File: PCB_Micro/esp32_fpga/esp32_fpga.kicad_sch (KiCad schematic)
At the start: 88 parts, among them IC1 ICE40UP5K-SG48I, J1 DM3AT-SF-PEJM5, J2 AUX1, J3 USB_C_Receptacle_USB2.0_16P, J4 Conn_01x04_Pin, J7 AUX2, J8 AUX3, Q1 DMP1045U-7, SW1 SW_Push, U1 ESP32-S3-WROOM-1-N8R8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

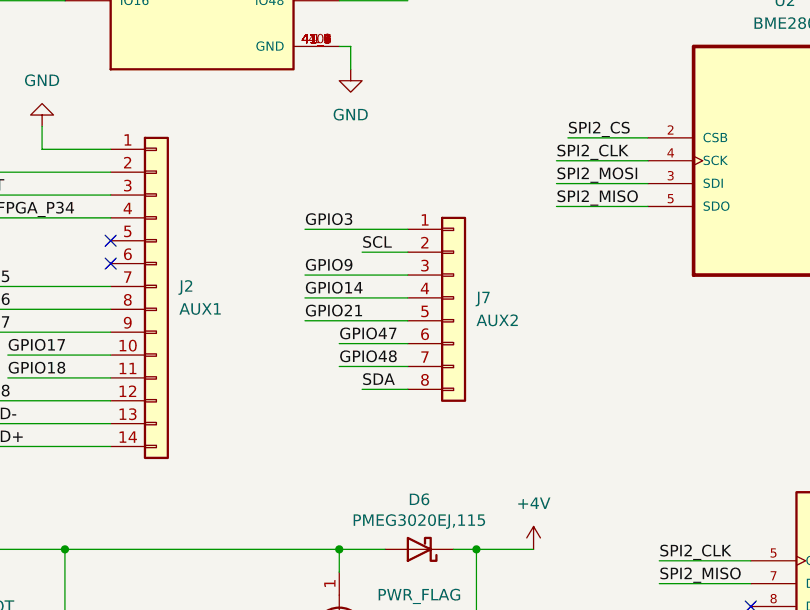
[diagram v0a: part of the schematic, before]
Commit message: PCB save agencement esp32
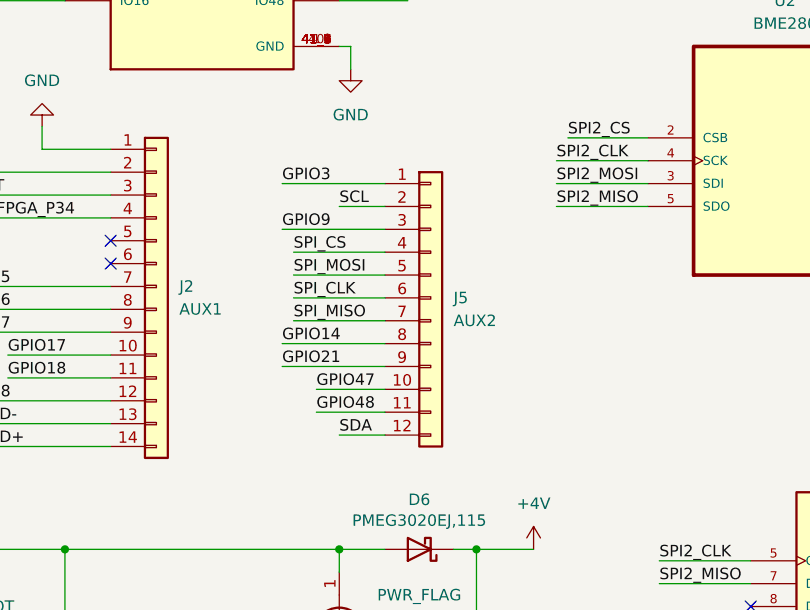
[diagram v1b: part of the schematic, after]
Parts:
- removed J7: AUX2, Connector_PinSocket_1.27mm:PinSocket_1x08_P1.27mm_Vertical, symbol Connector_Generic:Conn_01x08
- added J5: AUX2, Connector_PinSocket_1.00mm:PinSocket_1x12_P1.00mm_Vertical, symbol Connector_Generic:Conn_01x12
- TP1: value TestPoint -> SPI_MISO
- TP2: value TestPoint -> SPI_CLK
- TP3: value TestPoint -> SPI_CS
- TP4: value TestPoint -> SPI_MOSI
- TP5: value TestPoint -> CDONE
- TP6: value TestPoint -> CRESET
- TP7: value TestPoint -> VBATT
- TP8: value TestPoint -> GND
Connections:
- net GPIO14: now also J5.8 (Pin_8)
- net GPIO21: now also J5.9 (Pin_9)
- net GPIO3: now also J5.1 (Pin_1)
- net GPIO47: now also J5.10 (Pin_10)
- net GPIO48: now also J5.11 (Pin_11)
- net GPIO9: now also J5.3 (Pin_3)
- net SCL: now also J5.2 (Pin_2)
- net SDA: now also J5.12 (Pin_12)
- net SPI_CLK: now also J5.6 (Pin_6)
- net SPI_CS: now also J5.4 (Pin_4)
- net SPI_MISO: now also J5.7 (Pin_7)
- net SPI_MOSI: now also J5.5 (Pin_5)

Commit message: PCB presque terminé
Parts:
- added D8: LED_RGB, LED_SMD:LED_RGB_5050-6, symbol Device:LED_RGB
- J4: footprint Connector:NS-Tech_Grove_1x04_P2mm_Vertical -> Connector_PinHeader_2.00mm:PinHeader_1x04_P2.00mm_Vertical_SMD_Pin1Left
- TP1, TP2, TP3, TP4: footprint TestPoint:TestPoint_Pad_D1.0mm -> TestPoint:TestPoint_THTPad_1.0x1.0mm_Drill0.5mm
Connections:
- net PIN_P10: now also MK1.3 (WS)
- net PIN_P2: no longer MK1.1 (SCK)
- net PIN_P3: no longer MK1.2 (SD)
- net PIN_P4: no longer MK1.3 (WS)
- net PIN_P6: now also MK1.1 (SCK)
- net PIN_P9: now also MK1.2 (SD)
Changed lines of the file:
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@@
 		)
 	)
-	(label "PIN_P3"
+	(label "PIN_P9"
 		(at 265.43 40.64 180)
 		(effects
@@
 		)
 	)
-	(label "PIN_P4"
+	(label "PIN_P10"
 		(at 265.43 43.18 180)
 		(effects
@@
 		)
 	)
-	(label "PIN_P2"
+	(label "PIN_P6"
 		(at 265.43 38.1 180)
 		(effects
@@
 			)
 		)
-		(property "Footprint" "TestPoint:TestPoint_Pad_D1.0mm"
+		(property "Footprint" "TestPoint:TestPoint_THTPad_1.0x1.0mm_Drill0.5mm"
 			(at 234.95 252.73 0)
 			(effects
@@
 			)
 		)
-		(property "Footprint" "TestPoint:TestPoint_Pad_D1.0mm"
+		(property "Footprint" "TestPoint:TestPoint_THTPad_1.0x1.0mm_Drill0.5mm"
 			(at 234.95 247.65 0)
 			(effects
@@
 			)
 		)
-		(property "Footprint" "Connector:NS-Tech_Grove_1x04_P2mm_Vertical"
+		(property "Footprint" "Connector_PinHeader_2.00mm:PinHeader_1x04_P2.00mm_Vertical_SMD_Pin1Left"
 			(at 138.43 87.63 0)
 			(effects
@@
 	)
 	(symbol
+		(lib_id "Device:LED_RGB")
+		(at 351.79 220.98 0)
+		(unit 1)
+		(exclude_from_sim no)
+		(in_bom yes)
+		(on_board yes)
+		(dnp no)
+		(fields_autoplaced yes)
+		(property "Reference" "D8"
+			(at 351.79 207.01 0)
+			(effects
+				(font
+					(size 1.27 1.27)
+				)
+			)
+		)
+		(property "Value" "LED_RGB"
+			(at 351.79 209.55 0)
+			(effects
+				(font
+					(size 1.27 1.27)
+				)
+			)
+		)
+		(property "Footprint" "LED_SMD:LED_RGB_5050-6"
+			(at 351.79 222.25 0)
+			(effects
+				(font
+					(size 1.27 1.27)
+				)
+				(hide yes)
+			)
+		)
+		(property "Datasheet" "~"
+			(at 351.79 222.25 0)
+			(effects
+				(font
+					(size 1.27 1.27)
+				)
+				(hide yes)
+			)
+		)
+		(property "Description" "RGB LED, 6 pin package"
+			(at 351.79 220.98 0)
+			(effects
+				(font
+					(size 1.27 1.27)
+				)
+				(hide yes)
+			)
+		)
+		(pin "3"
+		)
+		(pin "1"
+		)
+		(pin "6"
+		)
+		(pin "5"
+		)
+		(pin "4"
+		)
+		(pin "2"
+		)
+		(instances
+			(project ""
+				(path "/e9b45eef-13aa-420c-803d-e39bf82057f5"
+					(reference "D8")
+					(unit 1)
+				)
+			)
+		)
+	)
+	(symbol
 		(lib_id "power:+3.3V")
 		(at 330.2 22.86 0)
@@
 			)
 		)
-		(property "Footprint" "TestPoint:TestPoint_Pad_D1.0mm"
+		(property "Footprint" "TestPoint:TestPoint_THTPad_1.0x1.0mm_Drill0.5mm"
 			(at 234.95 250.19 0)
 			(effects
@@
 			)
 		)
-		(property "Footprint" "TestPoint:TestPoint_Pad_D1.0mm"
+		(property "Footprint" "TestPoint:TestPoint_THTPad_1.0x1.0mm_Drill0.5mm"
 			(at 234.95 245.11 0)
 			(effects

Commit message: PCB rooté reste les erreurs a voir
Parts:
- removed J1: DM3AT-SF-PEJM5, custom:HRS_DM3AT-SF-PEJM5, symbol DM3AT-SF-PEJM5:DM3AT-SF-PEJM5
- removed TP1: SPI_MISO, TestPoint:TestPoint_THTPad_1.0x1.0mm_Drill0.5mm, symbol Connector:TestPoint
- removed TP2: SPI_CLK, TestPoint:TestPoint_THTPad_1.0x1.0mm_Drill0.5mm, symbol Connector:TestPoint
- removed TP3: SPI_CS, TestPoint:TestPoint_THTPad_1.0x1.0mm_Drill0.5mm, symbol Connector:TestPoint
- removed TP4: SPI_MOSI, TestPoint:TestPoint_THTPad_1.0x1.0mm_Drill0.5mm, symbol Connector:TestPoint
- removed TP5: CDONE, TestPoint:TestPoint_Pad_D1.0mm, symbol Connector:TestPoint
- removed TP6: CRESET, TestPoint:TestPoint_Pad_D1.0mm, symbol Connector:TestPoint
- added J6: 503398-1892, custom:5033981892, symbol 503398-1892:503398-1892
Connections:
- net +3.3V: now also J6.4 (VDD)
- net ADC: now also J2.4 (Pin_4)
- net CDONE: now also J2.8 (Pin_8)
- net CRESET: now also J2.9 (Pin_9)
- net GND: now also J6.11, J6.12, J6.13, J6.14, J6.6 (VSS)
- net GPIO5: now also J2.5 (Pin_5); no longer J2.7 (Pin_7)
- net GPIO6: now also J2.6 (Pin_6); no longer J2.8 (Pin_8)
- net GPIO7: now also J2.7 (Pin_7); no longer J2.9 (Pin_9)
- net SPI2_CLK: now also J6.5 (CLK)
- net SPI2_CS: now also J6.2 (CD/DAT3)
- net SPI2_MISO: now also J6.7 (DAT0)
- net SPI2_MOSI: now also J6.3 (CMD)
- net FPGA_P34: no longer names the net of IC1.34 (IOT_44B)
- net FPGA_P34: no longer J2.4 (Pin_4)
- no-connect marks 8 -> 7
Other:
- moved on the sheet: C11

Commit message: PCB terminé avec gerber sans LEDs niveau sonore
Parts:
- added SW2: SW_Push, Button_Switch_SMD:SW_SPST_PTS810, symbol Switch:SW_Push
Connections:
- net GND: now also SW2.2
- net GPIO0: now also SW2.1
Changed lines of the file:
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@@
 	(wire
 		(pts
+			(xy 25.4 53.34) (xy 25.4 57.15)
+		)
+		(stroke
+			(width 0)
+			(type default)
+		)
+	)
+	(wire
+		(pts
 			(xy 162.56 127) (xy 163.83 127)
 		)
@@
 	(wire
 		(pts
+			(xy 25.4 67.31) (xy 25.4 72.39)
+		)
+		(stroke
+			(width 0)
+			(type default)
+		)
+	)
+	(wire
+		(pts
 			(xy 62.23 133.35) (xy 72.39 133.35)
 		)
@@
 		)
 	)
+	(label "GPIO0"
+		(at 25.4 53.34 0)
+		(effects
+			(font
+				(size 1.27 1.27)
+			)
+			(justify left bottom)
+		)
+	)
 	(label "PIN_P48"
 		(at 201.93 72.39 180)
@@
 	)
 	(symbol
+		(lib_id "power:GND")
+		(at 25.4 72.39 0)
+		(mirror y)
+		(unit 1)
+		(exclude_from_sim no)
+		(in_bom yes)
+		(on_board yes)
+		(dnp no)
+		(property "Reference" "#PWR014"
+			(at 25.4 78.74 0)
+			(effects
+				(font
+					(size 1.27 1.27)
+				)
+				(hide yes)
+			)
+		)
+		(property "Value" "GND"
+			(at 25.273 76.7842 0)
+			(effects
+				(font
+					(size 1.27 1.27)
+				)
+			)
+		)
+		(property "Footprint" ""
+			(at 25.4 72.39 0)
+			(effects
+				(font
+					(size 1.27 1.27)
+				)
+				(hide yes)
+			)
+		)
+		(property "Datasheet" ""
+			(at 25.4 72.39 0)
+			(effects
+				(font
+					(size 1.27 1.27)
+				)
+				(hide yes)
+			)
+		)
+		(property "Description" ""
+			(at 25.4 72.39 0)
+			(effects
+				(font
+					(size 1.27 1.27)
+				)
+			)
+		)
+		(pin "1"
+		)
+		(instances
+			(project "esp32_fpga"
+				(path "/e9b45eef-13aa-420c-803d-e39bf82057f5"
+					(reference "#PWR014")
+					(unit 1)
+				)
+			)
+		)
+	)
+	(symbol
 		(lib_id "Device:LED_Small")
 		(at 213.36 182.88 90)
@@
 					(unit 1)
 				)
+			)
+		)
+	)
+	(symbol
+		(lib_id "Switch:SW_Push")
+		(at 25.4 62.23 90)
+		(mirror x)
+		(unit 1)
+		(exclude_from_sim no)
+		(in_bom yes)
+		(on_board yes)
+		(dnp no)
+		(property "Reference" "SW2"
+			(at 20.32 62.23 0)
+			(effects
+				(font
+					(size 1.27 1.27)
+				)
+			)
+		)
+		(property "Value" "SW_Push"
+			(at 20.4724 62.23 0)
+			(effects
+				(font
+					(size 1.27 1.27)
+				)
+				(hide yes)
+			)
+		)
+		(property "Footprint" "Button_Switch_SMD:SW_SPST_PTS810"
+			(at 20.32 62.23 0)
+			(effects
+				(font
+					(size 1.27 1.27)
+				)
+				(hide yes)
+			)
+		)
+		(property "Datasheet" "~"
+			(at 20.32 62.23 0)
+			(effects
+				(font
+					(size 1.27 1.27)
+				)
+				(hide yes)
+			)
+		)
+		(property "Description" ""
+			(at 25.4 62.23 0)
+			(effects
+				(font
+					(size 1.27 1.27)
+				)
+			)
+		)
+		(pin "1"
+		)
+		(pin "2"
+		)
+		(instances
+			(project "esp32_fpga"
+				(path "/e9b45eef-13aa-420c-803d-e39bf82057f5"
+					(reference "SW2")
+					(unit 1)
+				)

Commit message: Ajout de labels et modifications d'empreinte tjr sans LED
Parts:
- J4: footprint Connector_PinHeader_2.00mm:PinHeader_1x04_P2.00mm_Vertical_SMD_Pin1Left -> Connector_PinSocket_2.54mm:PinSocket_1x04_P2.54mm_Vertical
- PMOD1, PMOD2, PMOD3: footprint Connector_PinSocket_2.54mm:PinSocket_2x06_P2.54mm_Vertical -> Connector_Samtec_HLE_THT:Samtec_HLE-106-02-xx-DV-TE_2x06_P2.54mm_Horizontal
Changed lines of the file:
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@@
 			)
 		)
-		(property "Footprint" "Connector_PinSocket_2.54mm:PinSocket_2x06_P2.54mm_Vertical"
+		(property "Footprint" "Connector_Samtec_HLE_THT:Samtec_HLE-106-02-xx-DV-TE_2x06_P2.54mm_Horizontal"
 			(at 207.01 138.43 0)
 			(effects
@@
 			)
 		)
-		(property "Footprint" "Connector_PinSocket_2.54mm:PinSocket_2x06_P2.54mm_Vertical"
+		(property "Footprint" "Connector_Samtec_HLE_THT:Samtec_HLE-106-02-xx-DV-TE_2x06_P2.54mm_Horizontal"
 			(at 271.78 100.33 0)
 			(effects
@@
 			)
 		)
-		(property "Footprint" "Connector_PinHeader_2.00mm:PinHeader_1x04_P2.00mm_Vertical_SMD_Pin1Left"
+		(property "Footprint" "Connector_PinSocket_2.54mm:PinSocket_1x04_P2.54mm_Vertical"
 			(at 138.43 87.63 0)
 			(effects
@@
 			)
 		)
-		(property "Footprint" "Connector_PinSocket_2.54mm:PinSocket_2x06_P2.54mm_Vertical"
+		(property "Footprint" "Connector_Samtec_HLE_THT:Samtec_HLE-106-02-xx-DV-TE_2x06_P2.54mm_Horizontal"
 			(at 207.01 105.41 0)
 			(effects

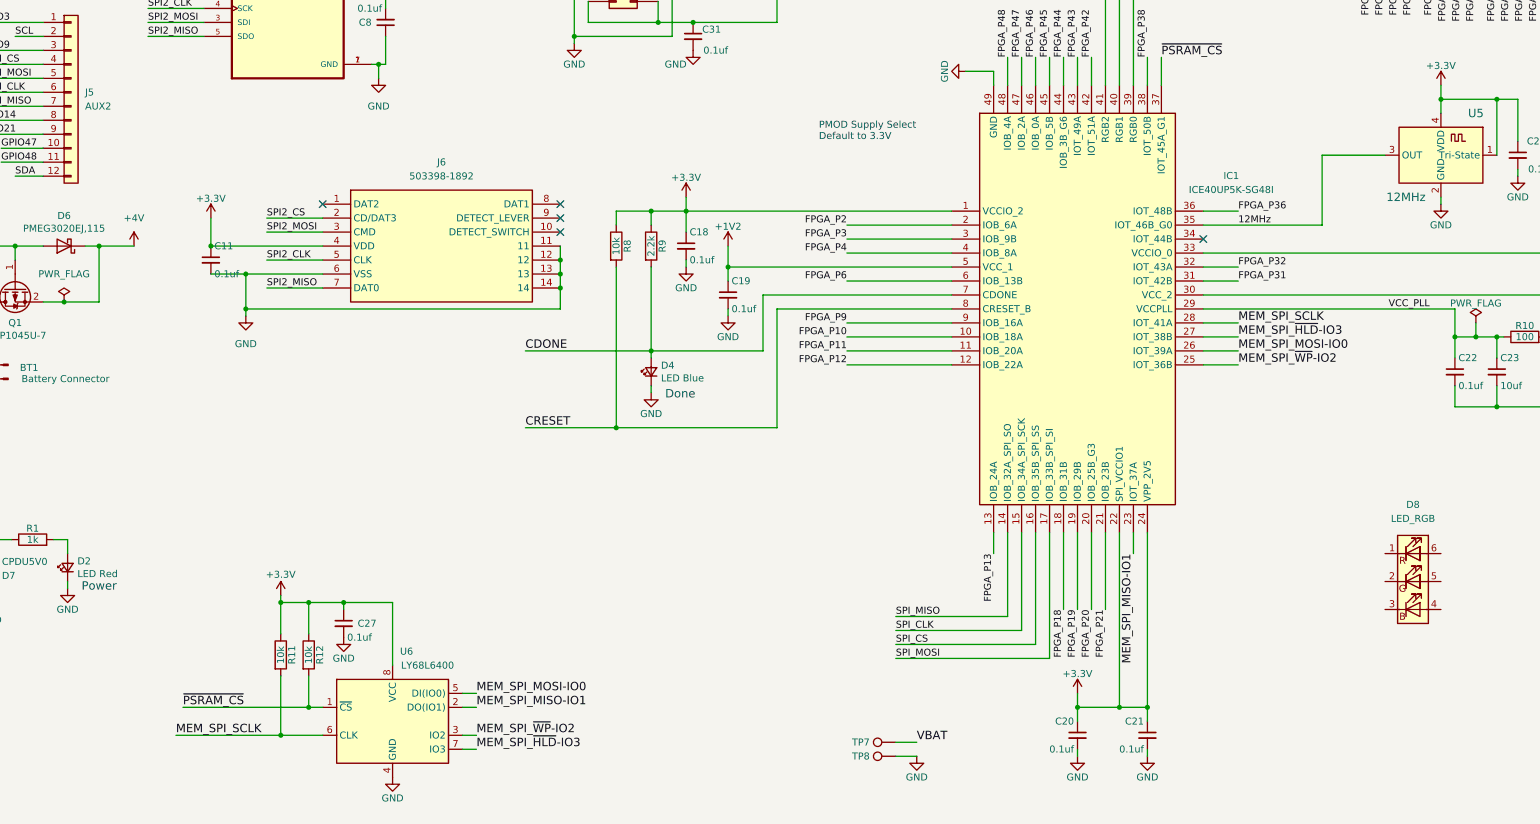
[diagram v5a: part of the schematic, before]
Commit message: PCB et schématique modifié pour l'implémentation de la LED RGB avec alim externe
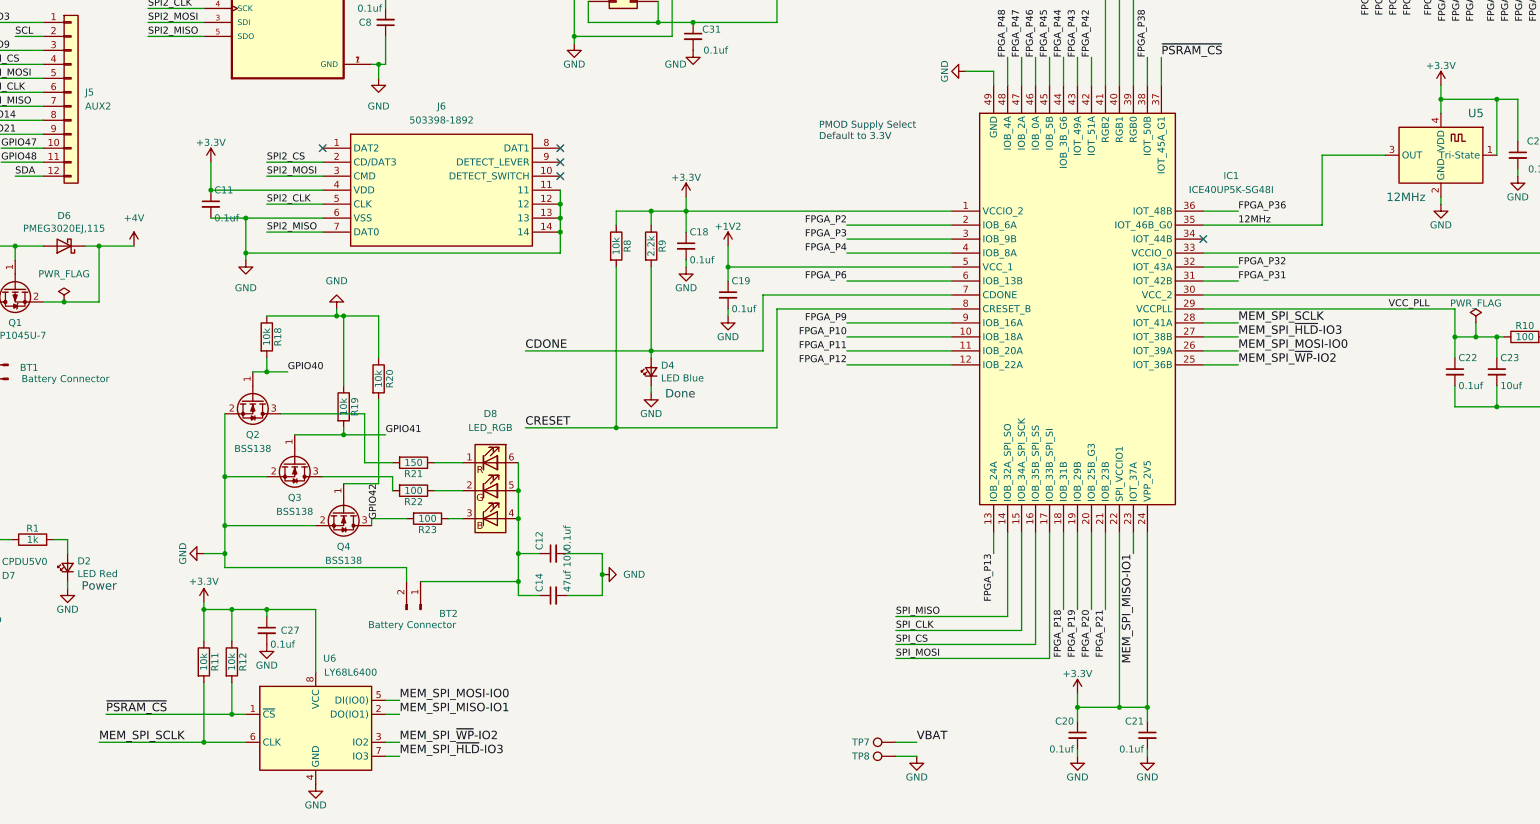
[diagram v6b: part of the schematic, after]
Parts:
- added BT2: Battery Connector, Connector_JST:JST_EH_B2B-EH-A_1x02_P2.50mm_Vertical, symbol Connector:Conn_01x02_Pin
- added C12: 0.1uf, Capacitor_SMD:C_0402_1005Metric, symbol Device:C_Small
- added C14: 47uf 10V, Capacitor_SMD:C_0402_1005Metric, symbol Device:C_Small
- added Q2, Q3, Q4: BSS138, Package_TO_SOT_SMD:SOT-23, symbol Transistor_FET:BSS138
- added R18, R19, R20: 10k, Resistor_SMD:R_0603_1608Metric, symbol Device:R
- added R21: 150, Resistor_SMD:R_0603_1608Metric, symbol Device:R
- added R22, R23: 100, Resistor_SMD:R_0603_1608Metric, symbol Device:R
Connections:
- net GND: now also BT2.2 (Pin_2), C12.2, C14.2, Q2.2 (S), Q3.2 (S), Q4.2 (S), R18.1, R19.1, R20.1
- net GPIO40: now also Q2.1 (G), R18.2
- net GPIO41: now also Q3.1 (G), R19.2
- net GPIO42: now also Q4.1 (G), R20.2
- net at D8.1 (RK): now also R21.1
- net at D8.2 (GK): now also R22.1
- net at D8.3 (BK): now also R23.1
- net at D8.4 (BA): now also D8.5 (GA), D8.6 (RA), BT2.1 (Pin_1), C12.1, C14.1
- new net: Q4.3 (D), R23.2
- new net: Q3.3 (D), R22.2
- new net: Q2.3 (D), R21.2
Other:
- moved on the sheet: C11, C27, D8, J6, R11, R12, U6
